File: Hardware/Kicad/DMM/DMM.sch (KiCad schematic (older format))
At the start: 2 parts

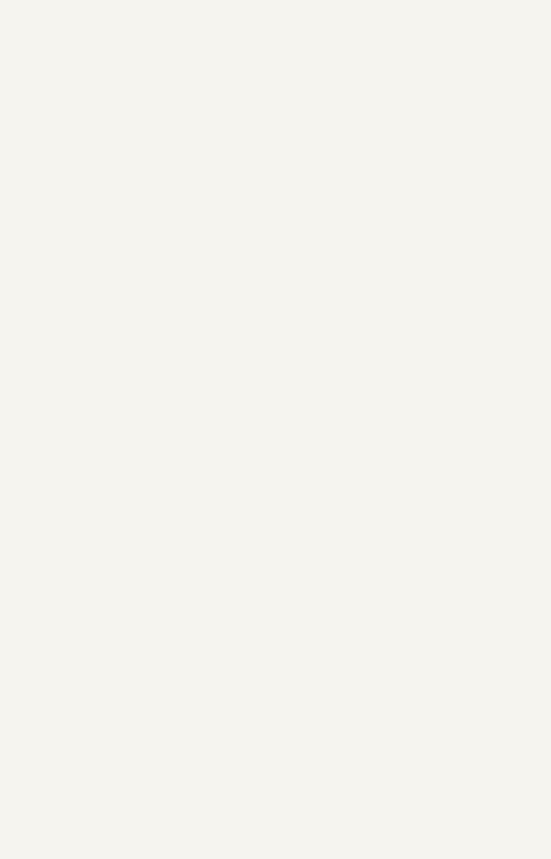
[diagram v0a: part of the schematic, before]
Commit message: Created ADS7521 sch lib file and added a new Data Converters Library
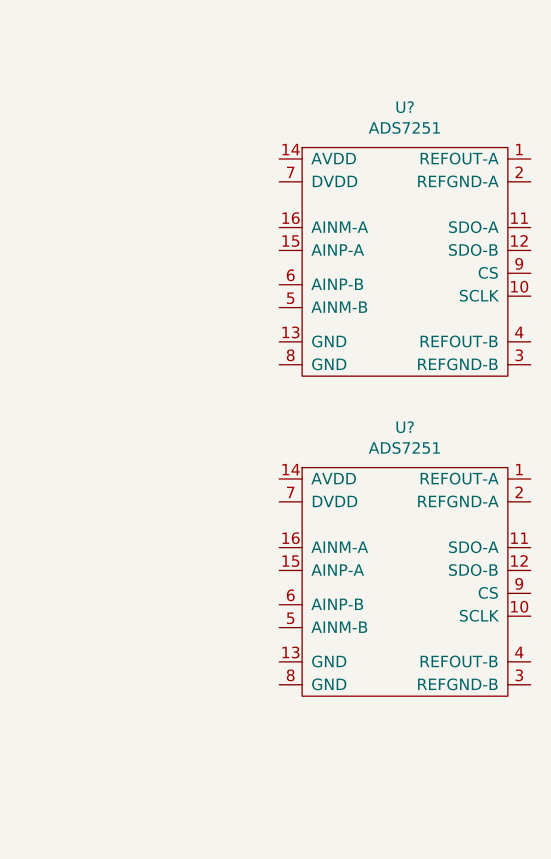
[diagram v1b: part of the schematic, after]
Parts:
- added U? (x2): ADS7251, symbol DBLS_Data_Converters:ADS7251
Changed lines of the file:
@@
+	1    0    0    -1
+$EndComp
+$Comp
+L DBLS_Data_Converters:ADS7251 U?
+U 1 1 5E6E6A61
+P 8000 1700
+F 0 "U?" H 8000 2325 50  0000 C CNN
+F 1 "ADS7251" H 8000 2234 50  0000 C CNN
+F 2 "" H 7750 2150 50  0001 C CNN
+F 3 "" H 7750 2150 50  0001 C CNN
+	1    8000 1700
+	1    0    0    -1
+$EndComp
+$Comp
+L DBLS_Data_Converters:ADS7251 U?
+U 1 1 5E6E81FB
+P 8000 3100
+F 0 "U?" H 8000 3725 50  0000 C CNN
+F 1 "ADS7251" H 8000 3634 50  0000 C CNN
+F 2 "" H 7750 3550 50  0001 C CNN
+F 3 "" H 7750 3550 50  0001 C CNN
+	1    8000 3100
 	1    0    0    -1
 $EndComp
